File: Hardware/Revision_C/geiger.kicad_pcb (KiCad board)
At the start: 2 copper layers, 84.7 x 31.9 mm, 28 parts, among them J1 I2C 5V, J2 I2C 3V3, J3 GND, U3 BSP125

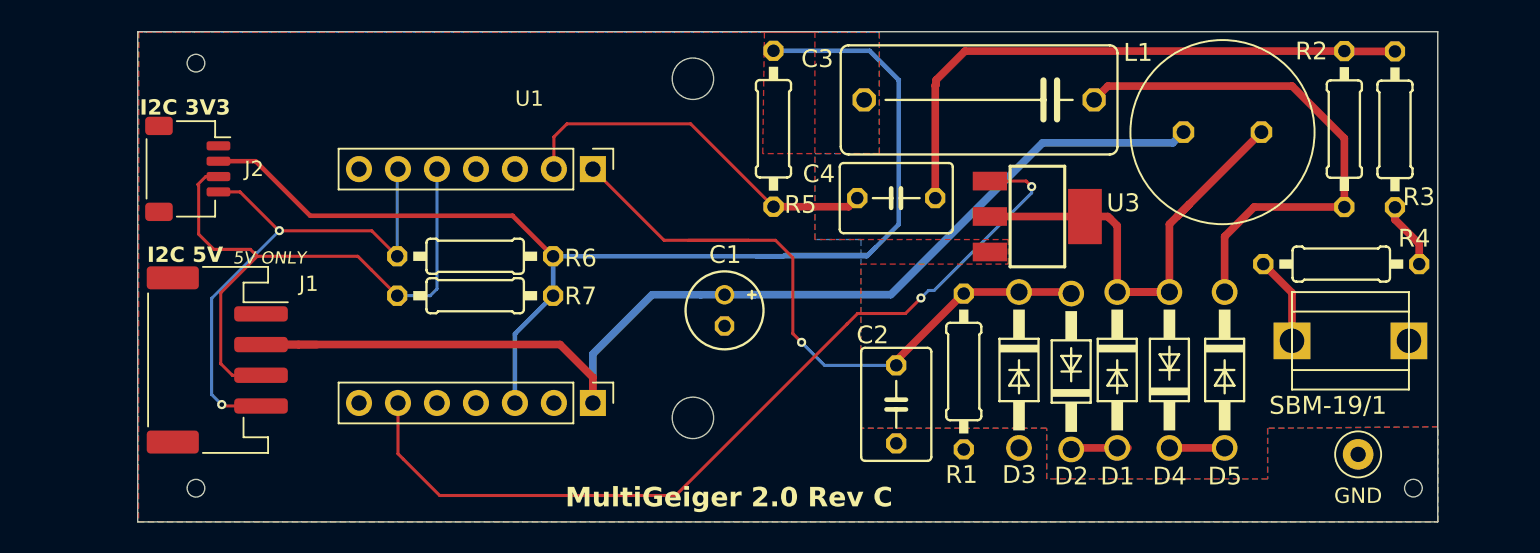
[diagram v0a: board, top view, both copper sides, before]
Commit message: Hardware: Rev B V2 + Rev C V2 — layout update to remove HV-to-counter crosstalk
Why these boards were redesigned:

The previous Rev B (Feather form factor) and Rev C (XIAO form factor)
carrier PCBs could register phantom Geiger counts: each pulse of the
high-voltage boost supply coupled a small spike into the tube counting
input. Long-term field data and bench probing traced the root cause to
the layout, not the circuit:

- The module socket pinout placed the counting input (GMZ_COUNT) directly
  beside the HV regulation sense net (HV_CAP_FUL), 2.54 mm pad to pad, so
  the most sensitive high-impedance node on the board (1 Mohm) was forced
  to run alongside its noisiest neighbour before routing even started.
- The counting trace crossed gaps in the ground plane (the worst void sat
  under the unused JP1 header on Rev B), weakening its return path exactly
  where the coupling occurred.

Firmware (V2.6.31+) fully compensates the phantom pulses by blanking, so
deployed nodes read correctly, but these V2 boards remove the coupling at
the source. What changed vs the previous revisions:

- Pin roles swapped at the module socket: GMZ_COUNT <-> HV_FET_OUT. The
  counting input now sits >=10 mm from both HV nets; the FET gate (a
  driven, low-impedance net) takes the seat next to the HV sense line.
- JP1 removed (Rev B), closing the ground-plane slot its through-holes cut.
- Routing rules enforced by DRC: >=2 mm clearance between the counting
  trace and both HV nets; crossings only on the opposite layer at 90 deg.
- Ground rebuilt: solid pours both sides with ~700 stitching vias; ground
  return coverage under the counting trace raised from ~79% to ~87%
  (Rev B; Rev C similar). The previous boards had no stitching vias near
  the counting run.
- Mounting holes enlarged 2.2 -> 2.7 mm to suit M2.5 hardware.
- The HV generation circuit itself is deliberately untouched: same
  schematic, same BOM, same tube chain.

IMPORTANT — FIRMWARE COMPATIBILITY: the pin-role swap makes b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
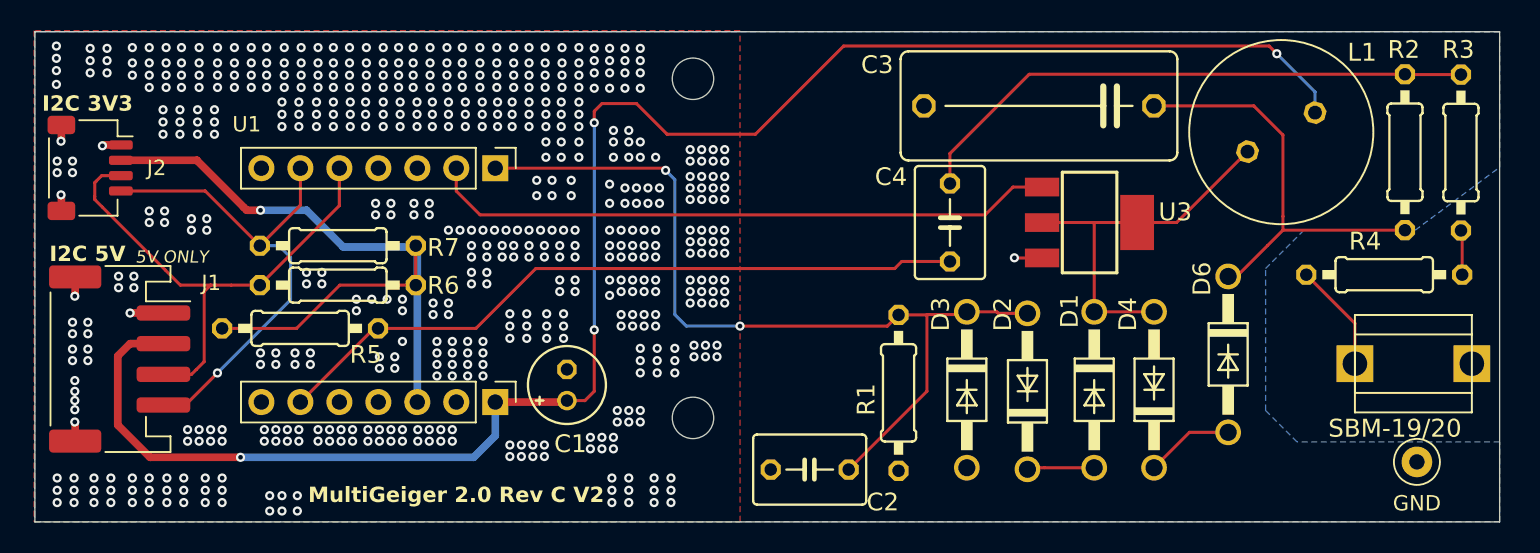
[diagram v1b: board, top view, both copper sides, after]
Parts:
- removed the REF** at (143.1, 124.2)
- removed the REF** at (175.5, 147.3)
- removed the REF** at (175.5, 125.2)
- removed the REF** at (143.1, 151.9)
- removed the REF** at (222.4, 151.8)
- added REF**: MountingHole_2.7mm_M2.5, MountingHole:MountingHole_2.7mm_M2.5, F.Cu at (175.5, 147.3)
- added REF**: MountingHole_2.7mm_M2.5, MountingHole:MountingHole_2.7mm_M2.5, F.Cu at (175.5, 125.2)
- moved R5 33.5 mm to (149.9, 141.4), turned to 0 degrees
- moved C1 11.4 mm to (167.3, 145.1), turned to 90 degrees
- moved R6 8.98 mm to (152.3, 138.6)
- moved R7 8.98 mm to (152.3, 136.0)
- moved C2 7.06 mm to (183.1, 150.6), turned to 180 degrees
- moved J2 6.36 mm to (136.2, 131.0)
- moved U1 6.36 mm to (155.0, 131.0)
- moved J1 6.36 mm to (138.1, 143.4)
- moved R3 4.56 mm to (225.5, 130.0)
- moved R1 4.47 mm to (188.9, 145.6)
- moved SBM-19/20 4.36 mm to (222.4, 144.4)
- moved R2 4.23 mm to (221.9, 130.0)
- moved C3 3.92 mm to (198.0, 126.9)
- moved J3 3.86 mm to (222.6, 150.1)
- moved C4 3.84 mm to (192.2, 134.5), turned to -90 degrees
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- renumbered D5 to D6, R7 to R6, R6 to R7, SBM-19/1 to SBM-19/20
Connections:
- U1 pad 2: /GMZ_COUNT -> /HV_FET_OUT
- U1 pad 9: /HV_FET_OUT -> /GMZ_COUNT
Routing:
- net +5V: track 76.8 -> 114.0 mm, vias 0 -> 4
- net +3V3: track 84.5 -> 48.2 mm, vias 0 -> 1
- net /GMZ_COUNT: track 24.1 -> 46.4 mm
- net /HV_FET_OUT: track 59.4 -> 40.6 mm, vias 2 -> 0
- net /HV_CAP_FUL: track 45.0 -> 56.7 mm, vias 1 -> 2
- net GND: track 0.00 -> 9.85 mm, vias 0 -> 571
- net Net-(D1-K): track 33.5 -> 25.0 mm
- net Net-(C3-Pad1): track 34.8 -> 28.5 mm
- net /SDA: track 40.9 -> 35.2 mm
- net Net-(D4-K): track 3.10 -> 5.79 mm
- net /SCL: track 35.1 -> 32.9 mm, vias 2 -> 1
- net Net-(R3-Pad2): track 4.35 -> 2.91 mm
- net Net-(SBM-19/1-1): track 5.77 -> 7.11 mm
- net Net-(D2-K): track 3.30 -> 4.53 mm
- net Net-(C4-Pad1): track 38.4 -> 37.7 mm
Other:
- board size 84.7 x 31.9 mm -> 95.5 x 31.9 mm
- board text added: "MultiGeiger 2.0 Rev C V2"
- board text removed: "MultiGeiger 2.0 Rev C"
